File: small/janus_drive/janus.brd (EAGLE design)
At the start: 33 x 33 mm, 27 parts, among them IC1 LM741

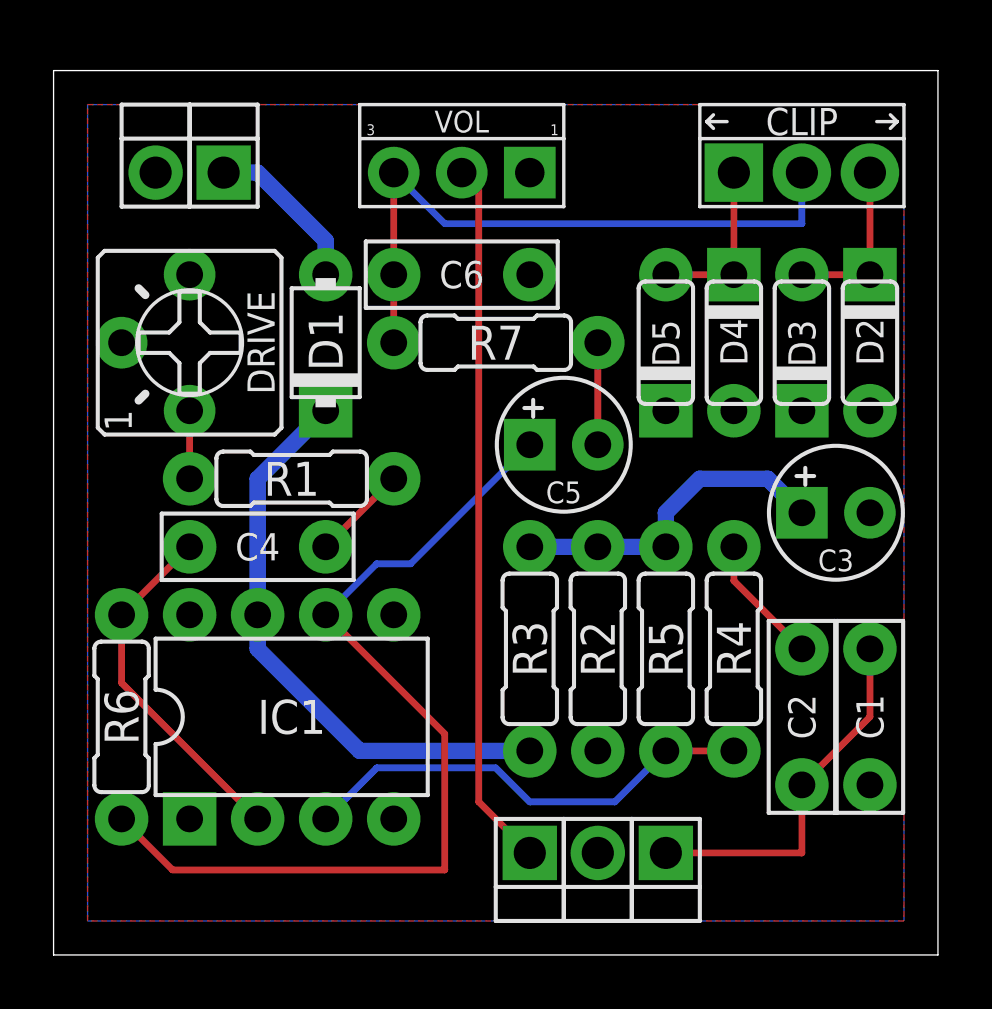
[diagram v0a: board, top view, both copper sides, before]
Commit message: updated Gaius Ringer & Janus Drive, added Chimera Chorus
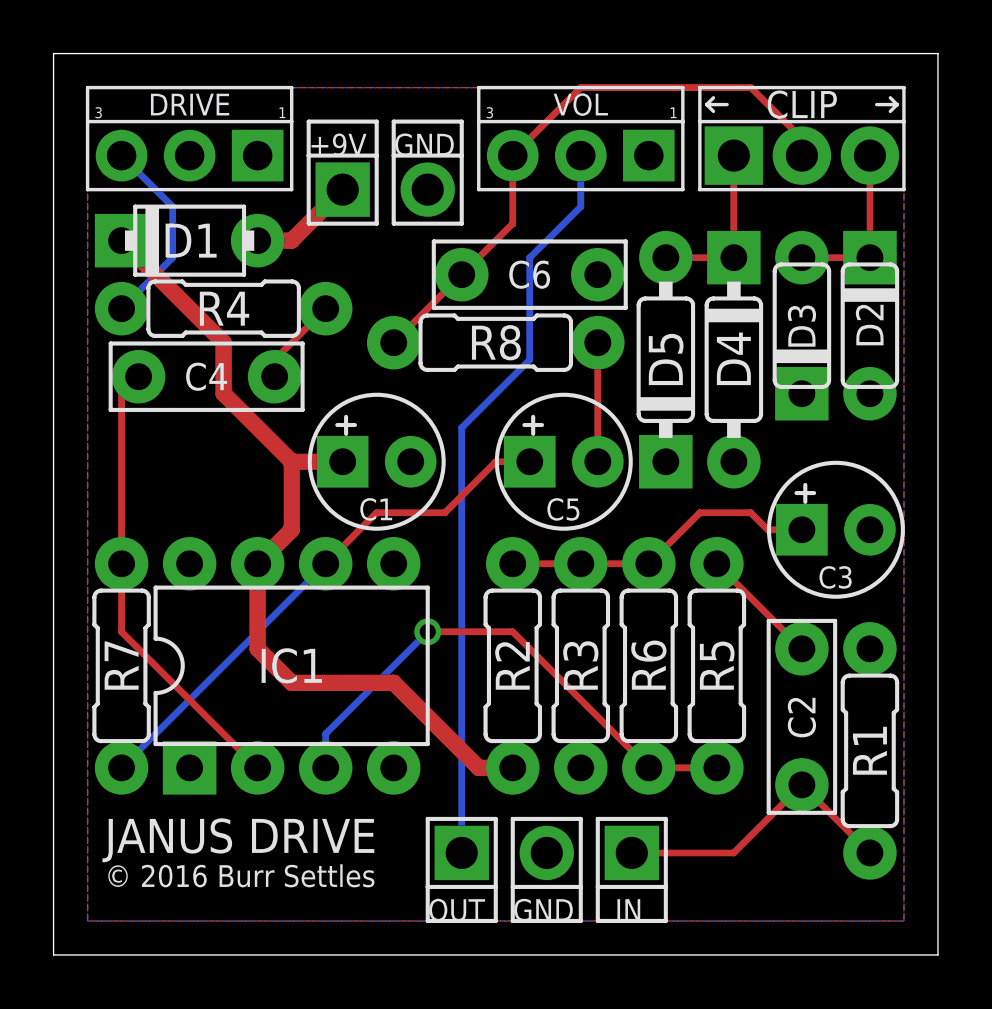
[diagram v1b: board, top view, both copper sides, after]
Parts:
- added R8: 10k, resistors:R0207/3
- C1: value 1nF -> 47u; device capacitors-film:BOX_SMALL -> capacitors-elec:050_020_1
- C2: value 10nF -> 10n
- C3: value 1uF (10uF) -> 10u
- C4: value 47nF -> 47n
- C5: value 1uF (10uF) -> 4u7
- C6: value 1nF -> 1n
- D1: value 1n5817 -> 1N5817
- D4, D5: device diodes:DO35-2 -> diodes:DO35-3
- DRIVE: value 50k -> 500kC; device potentiometers:2262_TRIM -> potentiometers:PADS_SMALL
- R1: value 4k7 (47k) -> 2M2
- R2, R3: value 1M (20k) -> 22k
- R4: value 10k -> 4k7
- R5: value 1M -> 10k
- R6: value 1M -> 470k
- R7: value 10k -> 1M
- moved PAD2 29.6 mm to (21.6, 3.81), turned to 0 degrees
- moved PAD1 27.5 mm to (10.8, 28.6), turned to 180 degrees
- moved R1 23.9 mm to (30.5, 7.62), turned to 270 degrees
- moved R4 22.9 mm to (6.35, 24.1), turned to 0 degrees
- moved C1 20.7 mm to (12.1, 18.4), turned to 0 degrees
- moved R6 19.8 mm to (22.2, 10.8), turned to 90 degrees
- moved R7 18.5 mm to (2.54, 10.8), turned to 270 degrees
- moved PAD4 10.2 mm to (14.0, 28.6)
- moved DRIVE 6.98 mm to (5.08, 29.8), turned to 0 degrees
- moved C4 6.63 mm to (5.71, 21.6)
- moved D1 6.35 mm to (5.08, 26.7), turned to 0 degrees
- moved VOL 4.49 mm to (19.7, 29.8)
- moved R2 3.24 mm to (17.1, 10.8), turned to 270 degrees
- moved C6 2.54 mm to (17.8, 25.4)
- moved PAD5 2.54 mm to (15.2, 3.81)
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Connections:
- net +9V: now also PAD1.1; no longer PAD2.1
- net CLIP: now also R8.2; no longer R7.2
- net GND: now also C1.-, DRIVE.1, R1.1, R3.1; no longer C1.1, DRIVE.3, R2.1
- net IN: now also PAD2.1, R1.2; no longer C1.2, PAD1.1
- net N$1: now also R5.1; no longer R4.1
- net N$10: now also DRIVE.3, R4.1; no longer DRIVE.1, R1.1
- net N$12: now also C1.+, R2.2; no longer R3.2
- net N$2: now also R5.2, R6.1; no longer R4.2, R5.1
- net N$3: now also R7.1; no longer R6.1
- net N$4: now also R4.2; no longer R1.2
- net N$5: now also R7.2; no longer R6.2
- net N$6: now also R8.1; no longer R7.1
- net N$8: now also R2.1, R3.2, R6.2; no longer R2.2, R3.1, R5.2
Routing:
- net N$5: track 34.5 -> 20.0 mm
- net N$12: track 21.7 -> 31.7 mm
- net N$10: track 2.54 -> 7.29 mm
- net N$3: track 13.3 -> 17.0 mm
- net IN: track 13.8 -> 11.0 mm
- net N$2: track 17.3 -> 19.6 mm, vias 0 -> 1
- net CLIP: track 24.3 -> 22.1 mm
- net +9V: track 6.13 -> 3.96 mm
- net OUT: track 26.5 -> 27.9 mm
- net N$6: track 3.81 -> 4.45 mm
- net N$8: track 12.5 -> 11.8 mm
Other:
- board size 33 x 33 mm -> 33 x 33.7 mm
- board text added: "+9V"
- board text added: "GND"
- board text added: "IN"
- board text added: "JANUS DRIVE"
- board text added: "OUT"
- board text added: "© 2016 Burr Settles"

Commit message: updates to a few small pedals
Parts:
- removed VOL: 100kA, potentiometers:PADS_SMALL
- added VOLUME: 100kA, potentiometers:PADS_SMALL
- C1: value 47u -> 2n2; device capacitors-elec:050_020_1 -> capacitors-film:BOX_SMALL
- C2: value 10n -> 47u; device capacitors-film:BOX_SMALL -> capacitors-elec:050_020_1
- C3: value 10u -> 10n; device capacitors-elec:050_020_1 -> capacitors-film:BOX_SMALL
- C4: value 47n -> 10u; device capacitors-film:BOX_SMALL -> capacitors-elec:050_020_1
- C5: value 4u7 -> 47n; device capacitors-elec:050_020_1 -> capacitors-film:BOX_SMALL
- C6: value 1n -> 4u7; device capacitors-film:BOX_SMALL -> capacitors-elec:050_020_1
- R1: value 2M2 -> 1M
- moved C4 20.5 mm to (26.0, 19.1), turned to 90 degrees
- moved C1 20.2 mm to (30.5, 10.2), turned to 270 degrees
- moved C2 19.4 mm to (11.4, 19.1), turned to 0 degrees
- moved C5 14.9 mm to (5.08, 23.5), turned to 90 degrees
- moved R8 13.4 mm to (29.8, 21.6), turned to 90 degrees
- moved D2 11.7 mm to (19.1, 21.0), turned to 0 degrees
- moved D4 10.3 mm to (15.9, 26.0), turned to 180 degrees
- moved D3 10.2 mm to (19.1, 18.4), turned to 180 degrees
- moved C6 8.28 mm to (26.0, 24.8), turned to 90 degrees
- moved CLIP 8.26 mm to (19.7, 29.8), flipped to the bottom
- moved D5 7.10 mm to (15.9, 23.5), turned to 0 degrees
- moved C3 5.85 mm to (27.9, 10.2), turned to 270 degrees
- moved R1 5.39 mm to (26.7, 3.81), turned to 180 degrees
- moved PAD2 5.08 mm to (16.5, 3.81)
- moved PAD3 5.08 mm to (13.3, 3.81)
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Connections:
- net CLIP: now also VOLUME.3; no longer C6.2, VOL.3
- net GND: now also C1.1, C2.-, C4.-, VOLUME.1; no longer C1.-, C3.-, C6.1, VOL.1
- net IN: now also C1.2, C3.2; no longer C2.2
- net N$1: now also C3.1; no longer C2.1
- net N$12: now also C2.+; no longer C1.+
- net N$3: now also C5.1; no longer C4.1
- net N$4: now also C5.2; no longer C4.2
- net N$5: now also C6.+; no longer C5.+
- net N$6: now also C6.-; no longer C5.-
- net N$8: now also C4.+; no longer C3.+
- net OUT: now also VOLUME.2; no longer VOL.2
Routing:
- net N$5: track 20.0 -> 39.0 mm
- net N$12: track 31.7 -> 20.3 mm
- net OUT: track 27.9 -> 36.0 mm
- net CLIP: track 22.1 -> 14.5 mm
- net IN: track 11.0 -> 17.7 mm
- net N$6: track 4.45 -> 9.83 mm
- net N$4: track 3.33 -> 8.67 mm
- net N$7: track 6.35 -> 11.7 mm
- net N$2: track 19.6 -> 15.4 mm, vias 1 -> 0
- net N$10: track 7.29 -> 3.81 mm
- net N$8: track 11.8 -> 10.6 mm
- net N$9: track 6.35 -> 7.40 mm
- net +9V: track 3.96 -> 4.49 mm
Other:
- board text added: "© 2016 burr settles"
- board text removed: "© 2016 Burr Settles"

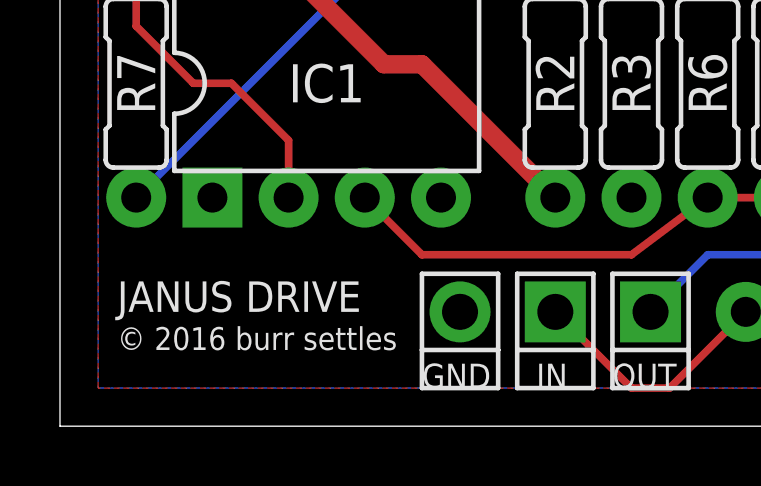
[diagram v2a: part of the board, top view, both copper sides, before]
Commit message: added phaser schematic; minor board tweaks
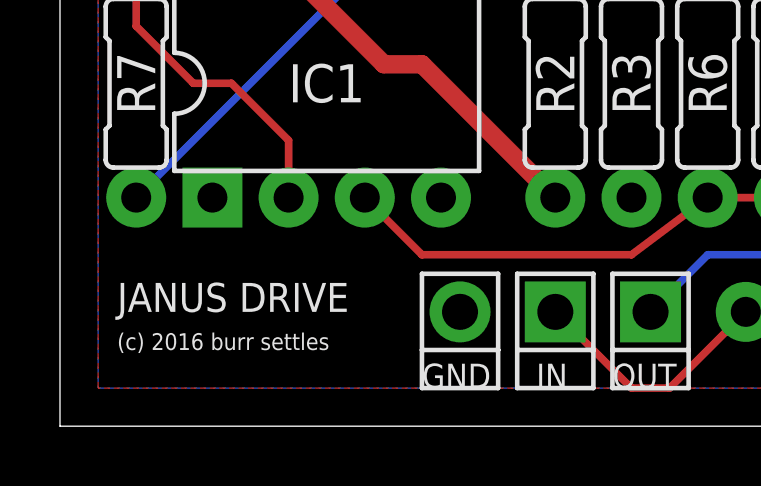
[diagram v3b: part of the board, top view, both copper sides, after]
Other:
- board text added: "(c) 2016 burr settles"
- board text removed: "© 2016 burr settles"
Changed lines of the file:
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@@
 <text x="12.065" y="1.27" size="0.8128" layer="25">GND</text>
 <text x="15.875" y="1.27" size="0.8128" layer="25">IN</text>
-<text x="1.905" y="3.81" size="1.016" layer="25">JANUS DRIVE</text>
-<text x="1.905" y="2.54" size="0.762" layer="25">© 2016 burr settles</text>
+<text x="1.905" y="3.81" size="0.9652" layer="25" font="vector">JANUS DRIVE</text>
+<text x="1.905" y="2.54" size="0.5588" layer="25" font="vector">(c) 2016 burr settles</text>
 </plain>
 <attributes>
